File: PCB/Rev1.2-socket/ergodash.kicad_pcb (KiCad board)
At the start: 2 copper layers, 149.9 x 127.4 mm, 86 parts, among them J1 5PIN, M1 Speaker, SW1 SW_PUSH, SW10 SW_PUSH, SW11 SW_PUSH, SW12 SW_PUSH, SW13 SW_PUSH, SW14 SW_PUSH, SW15 SW_PUSH, SW16 SW_PUSH, SW17 SW_PUSH, SW18 SW_PUSH, SW19 SW_PUSH, SW2 SW_PUSH, SW20 SW_PUSH, SW21 SW_PUSH, SW22 SW_PUSH, SW23 SW_PUSH, SW24 SW_PUSH, SW25 SW_PUSH, SW26 SW_PUSH, SW27 SW_PUSH, SW28 SW_PUSH, SW29 SW_Push, SW3 SW_PUSH, SW30 SW_PUSH, SW31 SW_PUSH, SW32 SW_PUSH, SW33 SW_PUSH, SW34 SW_PUSH, SW35 SW_PUSH, SW4 SW_PUSH, SW40 SW_PUSH, SW5 SW_PUSH, SW6 SW_PUSH, SW7 SW_PUSH, SW8 SW_PUSH, SW9 SW_PUSH, U1 HOLE, U2 HOLE, U3 ProMicro, U4 HOLE, U5 HOLE, U7 HOLE, U8 HOLE, U9 HOLE

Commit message: Finish left board routing and modernize solder mask clearance
Final GND island link routed in the GUI completes the board:
0 unconnected, 0 shorts, 0 clearance violations, and the pad
connectivity matches the schematic netlist exactly (all 55 nets).

Change pad_to_mask_clearance from the KiCad 5 era 0.2mm to 0 so
mask apertures no longer merge between nearby pads; this also
restores a solder dam in the tight SW13/U3 corridor. Remaining
DRC notes are accepted by design: U3 pin holes inside socket
courtyards (controller under the keys), positioning holes inside
courtyards, and one col6 track passing under the SW25 socket body.

Co-Authored-By: Claude Fable 5 <noreply@anthropic.com>
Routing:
- net /RX: track 37.6 -> 0.51 mm
- net GND: track 157.9 -> 165.8 mm
- net /rst: track 23.0 -> 16.1 mm
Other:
- rule pad_to_mask_clearance: 0.2 -> 0
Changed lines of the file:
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@@
 	)
 	(setup
-		(pad_to_mask_clearance 0.2)
+		(pad_to_mask_clearance 0)
 		(allow_soldermask_bridges_in_footprints no)
 		(tenting
@@
 	)
 	(segment
-		(start 149.225 40.767)
-		(end 148.082 39.624)
-		(width 0.254)
-		(layer "F.Cu")
-		(net "/rst")
-	)
-	(segment
-		(start 149.225 42.926)
-		(end 149.225 40.767)
-		(width 0.254)
-		(layer "F.Cu")
-		(net "/rst")
-	)
-	(segment
-		(start 149.225 42.926)
-		(end 150.749 44.45)
-		(width 0.254)
-		(layer "F.Cu")
-		(net "/rst")
-	)
-	(segment
 		(start 158.369 39.624)
 		(end 160.314 39.624)
@@
 	)
 	(segment
-		(start 151.765 44.45)
-		(end 150.749 44.45)
-		(width 0.254)
-		(layer "F.Cu")
-		(net "/rst")
-	)
-	(segment
 		(start 156.464 44.45)
 		(end 157.48 43.434)
@@
 	)
 	(segment
-		(start 142.494 42.037)
-		(end 142.494 40.6)
-		(width 0.254)
-		(layer "F.Cu")
-		(net "GND")
-	)
-	(segment
-		(start 140.081 44.45)
-		(end 136.525 44.45)
-		(width 0.254)
-		(layer "F.Cu")
-		(net "GND")
-	)
-	(segment
 		(start 168.783 40.64)
 		(end 166.33 40.64)
@@
 	)
 	(segment
-		(start 142.494 42.037)
-		(end 140.081 44.45)
-		(width 0.254)
-		(layer "F.Cu")
-		(net "GND")
-	)
-	(segment
 		(start 179.411 45.172)
 		(end 179.411 45.72)
@@
 	)
 	(segment
+		(start 145.597454 41.91)
+		(end 151.765 41.91)
+		(width 0.254)
+		(layer "B.Cu")
+		(net "GND")
+	)
+	(segment
 		(start 158.55763 43.815)
 		(end 161.123 43.815)
@@
 	)
 	(segment
+		(start 136.525 44.45)
+		(end 143.057454 44.45)
+		(width 0.254)
+		(layer "B.Cu")
+		(net "GND")
+	)
+	(segment
+		(start 143.057454 44.45)
+		(end 145.597454 41.91)
+		(width 0.254)
+		(layer "B.Cu")
+		(net "GND")
+	)
+	(segment
 		(start 151.765 41.91)
 		(end 155.575 41.91)
@@
 	)
 	(segment
-		(start 137.033 41.91)
-		(end 140.97 37.973)
-		(width 0.254)
-		(layer "B.Cu")
-		(net "/RX")
-	)
-	(segment
-		(start 140.97 37.973)
-		(end 165.862 37.973)
-		(width 0.254)
-		(layer "B.Cu")
-		(net "/RX")
-	)
-	(segment
-		(start 165.862 37.973)
-		(end 169.799 41.91)
-		(width 0.254)
-		(layer "B.Cu")
-		(net "/RX")
-	)
-	(segment
-		(start 169.799 41.91)
-		(end 170.815 41.91)
-		(width 0.254)
-		(layer "B.Cu")
-		(net "/RX")
-	)
-	(segment

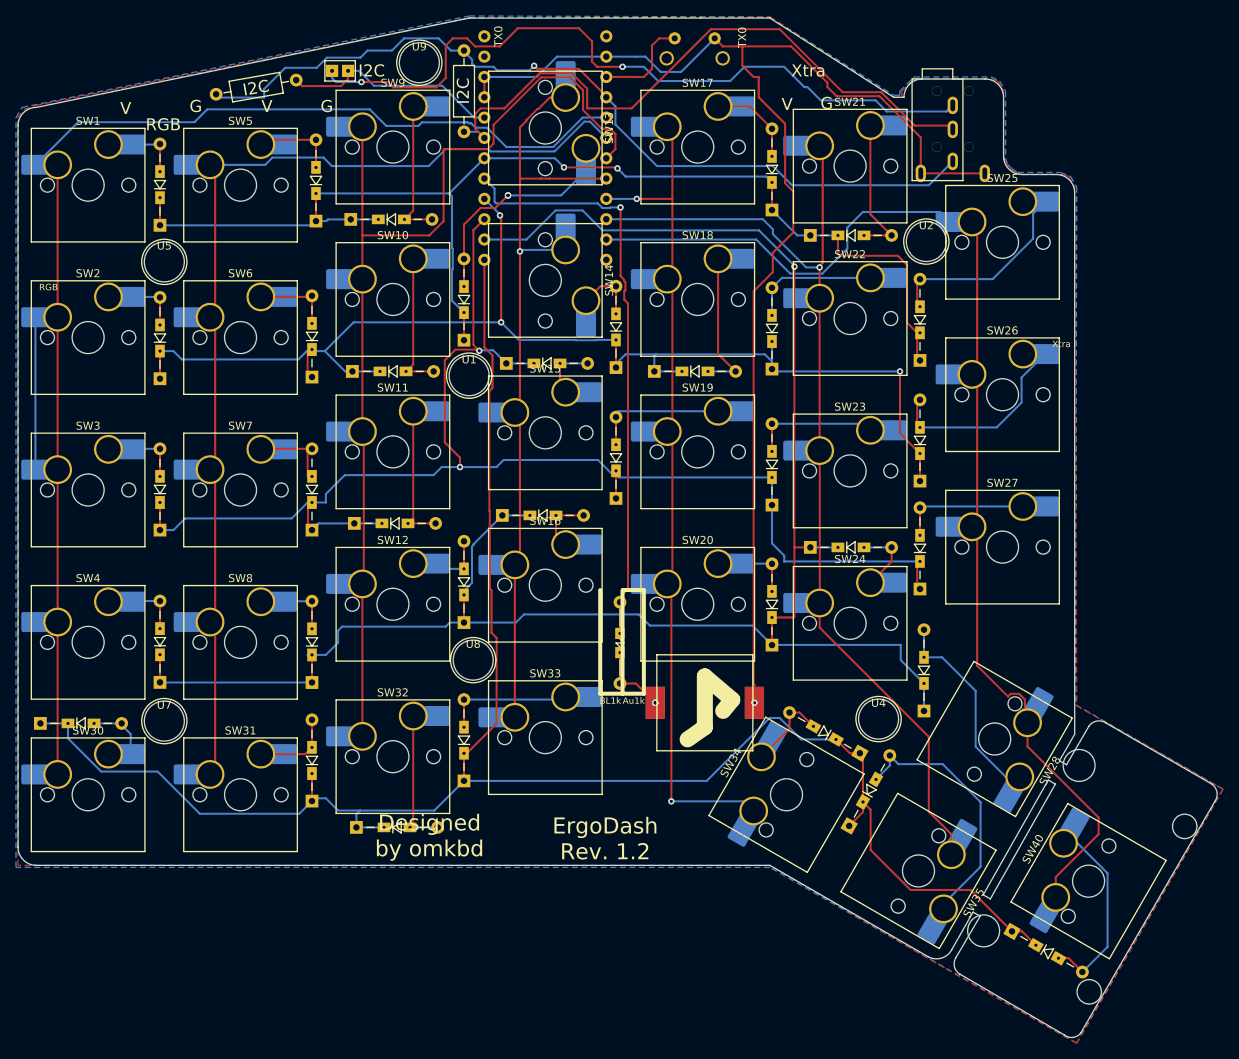
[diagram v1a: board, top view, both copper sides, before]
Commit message: Remove I2C/speaker options, add mascot logo, regenerate gerbers
- Remove the unpopulated I2C provision (pull-ups R1/R2, jumper W1) from
  schematic and board with its dead copper; split communication is QMK
  serial only (split.serial pin D0 = /sda/uart)
- Remove speaker M1 and its 1k resistor R40 (undocumented option absent
  from the build guide and shop list)
- Delete orphaned silk labels of removed options (V/G/RGB/I2C/Xtra/TX0/
  BL1k/Au1k); only the two nameplates remain, now reading
  "ErgoDash Rev. 1.2 / Socketed by tsubu" (also fixes the "Soket" typo)
- Restore bottom-row socket references SW30-SW35 that had drifted one
  step from the schematic (duplicate SW29, missing SW35)
- Add mascot logo footprint on both silkscreen sides and GND/VCC zones
- Regenerate manufacturing data into ergodash/ (verified in GerbView);
  drop the stale Rev1.2 gerber copies, originals live in PCB/Rev1.2/

Co-Authored-By: Claude Fable 5 <noreply@anthropic.com>
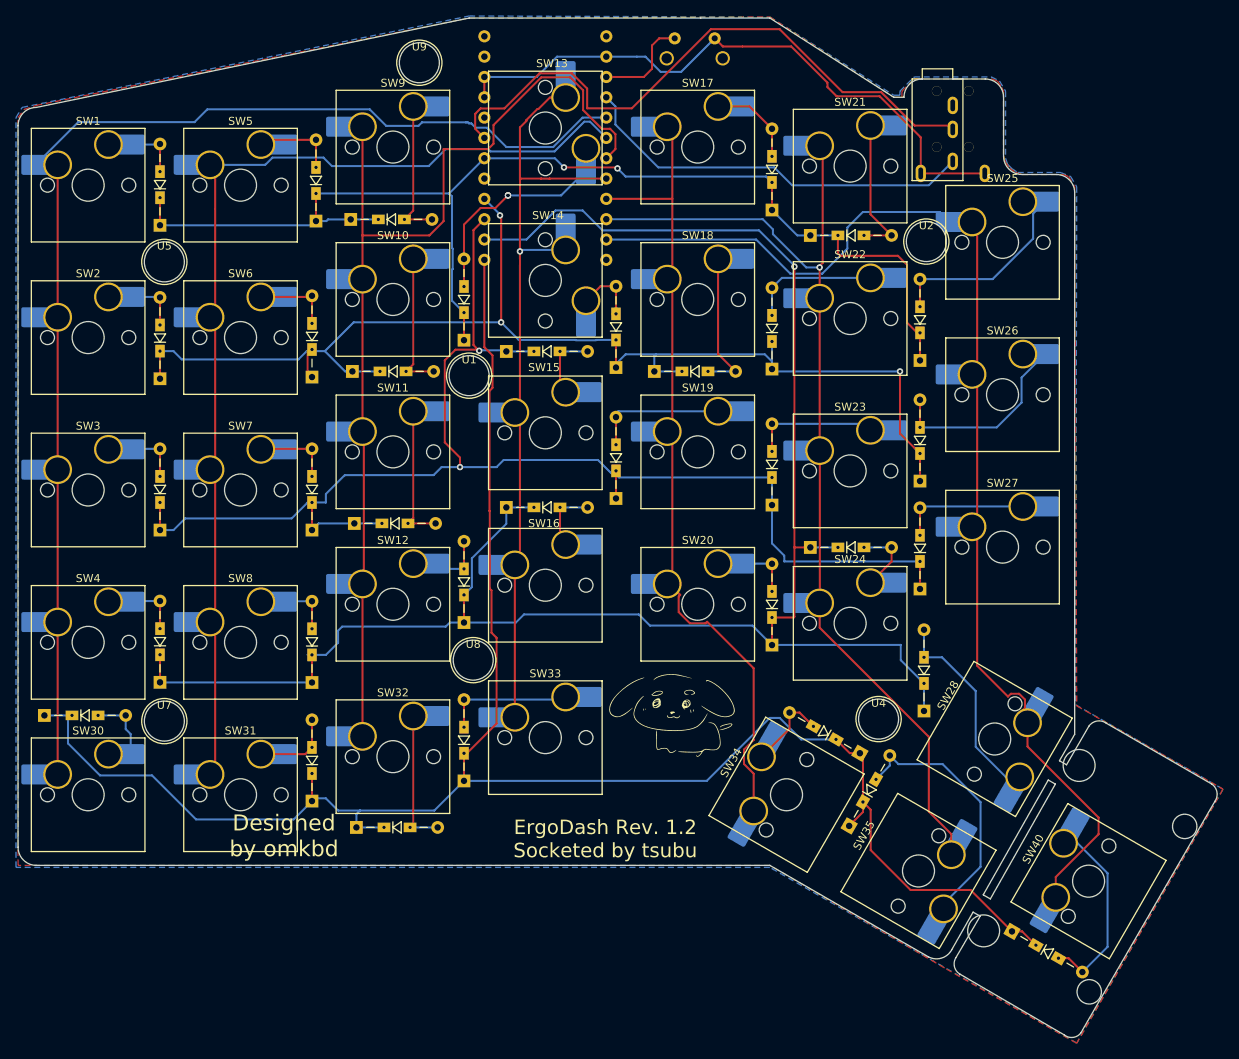
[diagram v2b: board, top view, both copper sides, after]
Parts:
- removed M1: Speaker, library:PKLCS1212E4001-R1
- removed R1, R2: R, library:R_Axial_DIN0207_L6.3mm_D2.5mm_P10.16mm_Horizontal
- removed R40: 1k, library:Resistors_SMD_THT
- removed W1: jumper_smd, library:jumper_smd_2dub
- added ?: LOGO, myfootprint:logo, F.Cu at (160.1, 123.0)
- added ?: LOGO, myfootprint:logo, B.Cu at (161.5, 124.8)
- moved D15 1.50 mm to (139.3, 78.8)
- moved D16 1.12 mm to (139.3, 98.3)
- moved D29 1.12 mm to (81.5, 124.3)
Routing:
- net /xtradata: track 92.7 -> 0.00 mm, vias 2 -> 0
- net GND: track 165.8 -> 78.6 mm, vias 1 -> 0
- net /Audio: track 73.7 -> 0.00 mm, vias 1 -> 0
- net VCC: track 107.0 -> 50.5 mm, vias 1 -> 0
- net /scl: track 27.8 -> 0.00 mm
- net /col0: track 173.3 -> 154.3 mm
- net Net-(M1-Audio): track 9.54 -> 0.00 mm, vias 2 -> 0
- net /rst: track 16.1 -> 12.3 mm
- net /sda/uart: track 80.9 -> 77.8 mm
- net /row4: track 235.9 -> 238.1 mm
- net Net-(D15-A): track 7.34 -> 8.84 mm
- net /row3: track 232.0 -> 233.2 mm
- net /col4: track 105.3 -> 106.1 mm, vias 2 -> 0
- net Net-(D16-A): track 9.57 -> 10.3 mm
- net /RX: track 0.51 -> 0.00 mm
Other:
- board text added: "ErgoDash Rev. 1.2 Socketed by tsubu"
- board text removed: "Au1k"
- board text removed: "BL1k"
- board text removed: "ErgoDash Rev. 1.2"
- board text removed: "G"
- board text removed: "I2C"
- board text removed: "RGB"
- board text removed: "TX0"
- board text removed: "V"
- board text removed: "Xtra"
